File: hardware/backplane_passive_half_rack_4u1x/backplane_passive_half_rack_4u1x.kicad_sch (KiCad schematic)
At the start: 0 parts

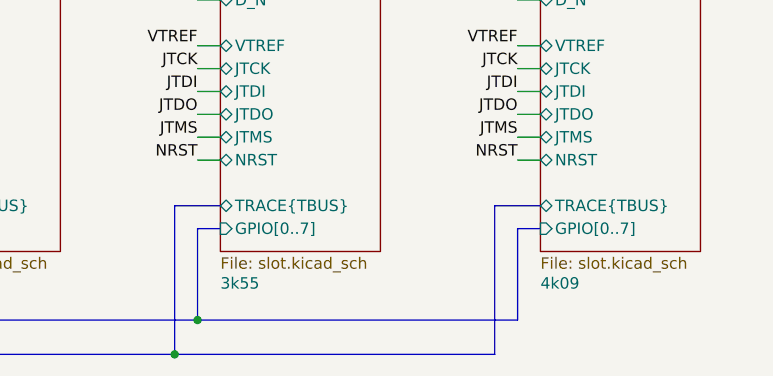
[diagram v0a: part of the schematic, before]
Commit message: Updated the RAddr values. Made USB a diff pair.
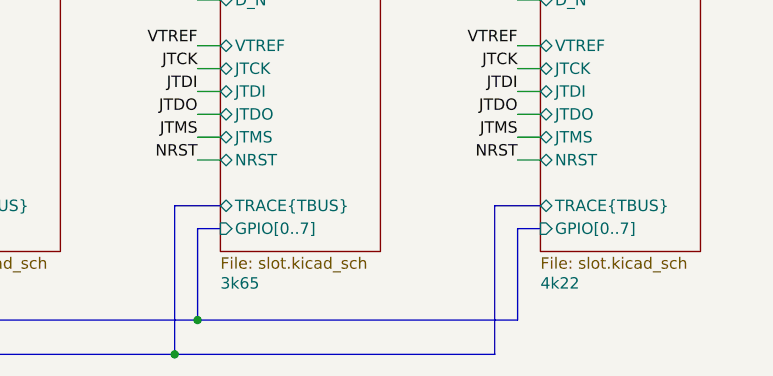
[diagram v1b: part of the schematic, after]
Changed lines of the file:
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@@
 			)
 		)
-		(property "RAddr" "3k55"
+		(property "RAddr" "3k65"
 			(at 193.04 141.224 0)
 			(show_name yes)
@@
 			)
 		)
-		(property "RAddr" "4k09"
+		(property "RAddr" "4k22"
 			(at 228.6 141.224 0)
 			(show_name yes)
